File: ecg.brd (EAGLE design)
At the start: 56 x 85 mm, 1 part

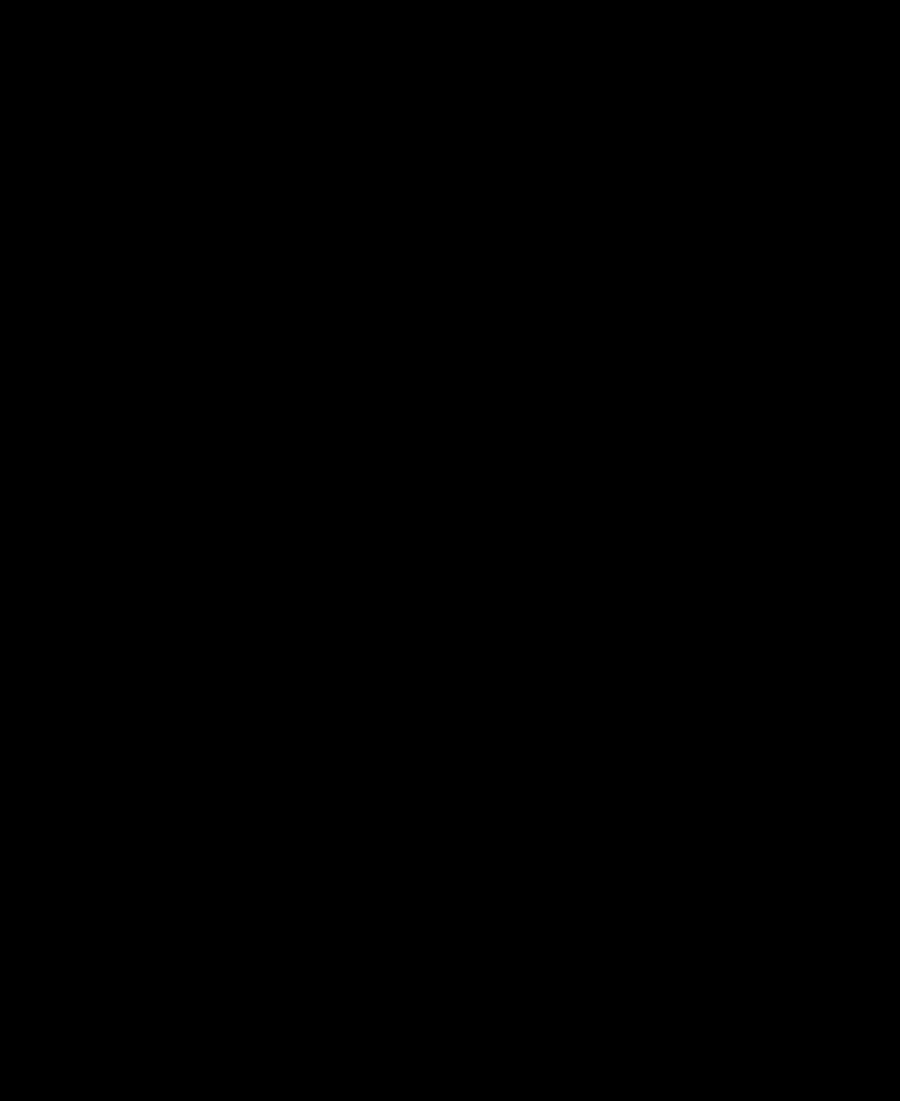
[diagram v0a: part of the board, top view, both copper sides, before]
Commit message: Added TMP102 and ADAS1000 to schematics
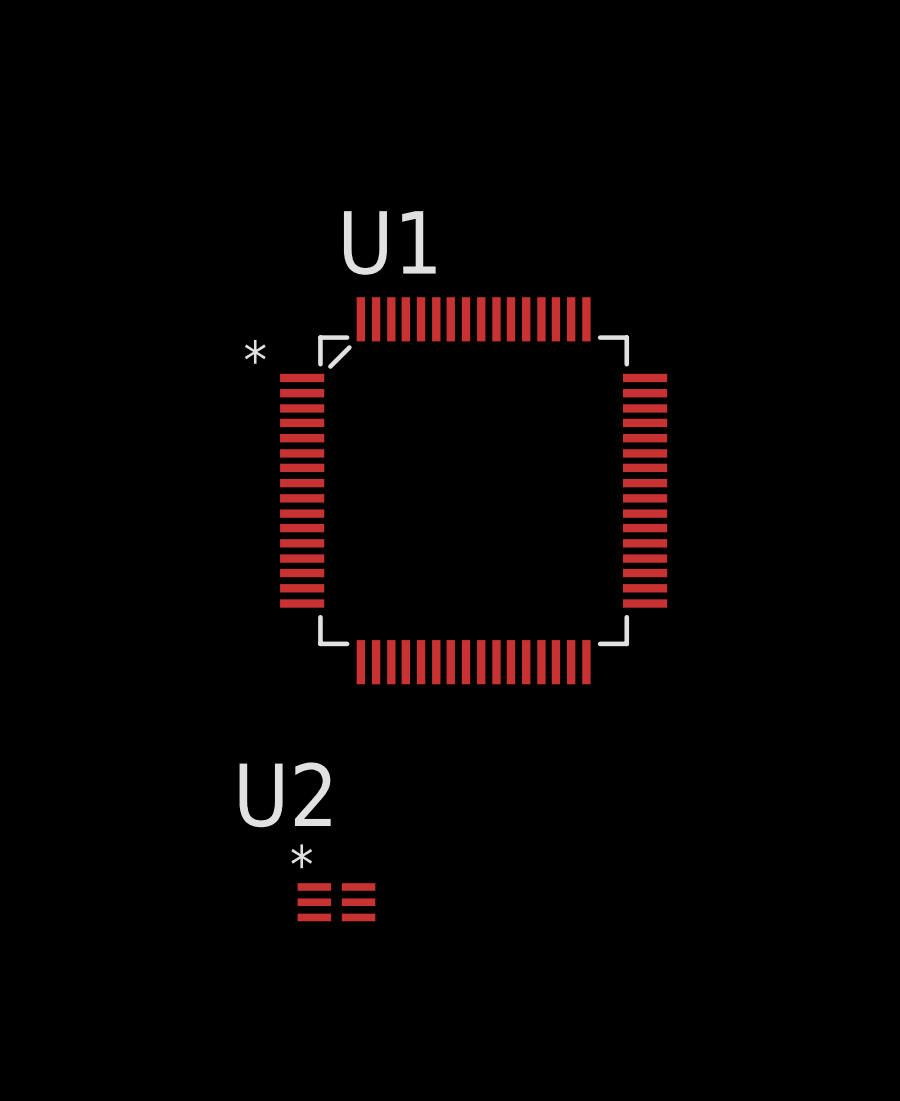
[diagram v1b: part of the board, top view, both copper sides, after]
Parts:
- added U1: ADAS1000-2BSTZ, ADAS1000:QFN50P1200X1200X160-64N
- added U2: TMP102AIDRLT, TMP102:SOT50P160X60-6N
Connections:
- new net !PD: U1.53
- new net ADCVDD: U1.26
- new net ADCVDD_2: U1.55
- new net AVDD: U1.58
- new net AVDD_2: U1.18
- new net AVDD_3: U1.63
- new net AVDD_4: U1.23
- new net DVDD: U1.51
- new net DVDD_2: U1.30
- new net IOVDD: U1.46
- new net IOVDD_2: U1.35
- new net V+: U2.5
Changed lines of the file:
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@@
 <elements>
 <element name="U$1" library="microbuilder" package="RASBERRYPI_SHIELD" value="RASPBERRYPI_BB" x="0" y="0"/>
+<element name="U1" library="ADAS1000" package="QFN50P1200X1200X160-64N" value="ADAS1000-2BSTZ" x="23.114" y="54.356">
+<attribute name="PACKAGE" value="LQFP-64" x="23.114" y="54.356" size="1.778" layer="27" display="off"/>
+<attribute name="OC_NEWARK" value="52W9262" x="23.114" y="54.356" size="1.778" layer="27" display="off"/>
+<attribute name="MPN" value="ADAS1000-2BSTZ " x="23.114" y="54.356" size="1.778" layer="27" display="off"/>
+<attribute name="SUPPLIER" value="ANALOG DEVICES " x="23.114" y="54.356" size="1.778" layer="27" display="off"/>
+<attribute name="OC_FARNELL" value="2254936" x="23.114" y="54.356" size="1.778" layer="27" display="off"/>
+</element>
+<element name="U2" library="TMP102" package="SOT50P160X60-6N" value="TMP102AIDRLT" x="18.542" y="40.64">
+<attribute name="PACKAGE" value="SOT-23-6" x="18.542" y="40.64" size="1.778" layer="27" display="off"/>
+<attribute name="OC_NEWARK" value="53M3987" x="18.542" y="40.64" size="1.778" layer="27" display="off"/>
+<attribute name="MPN" value="TMP102AIDRLT" x="18.542" y="40.64" size="1.778" layer="27" display="off"/>
+<attribute name="SUPPLIER" value="Texas Instruments" x="18.542" y="40.64" size="1.778" layer="27" display="off"/>
+<attribute name="OC_FARNELL" value="1652477" x="18.542" y="40.64" size="1.778" layer="27" display="off"/>
+</element>
 </elements>
 <signals>
+<signal name="AVDD_2">
+<contactref element="U1" pad="18"/>
+</signal>
+<signal name="AVDD_3">
+<contactref element="U1" pad="63"/>
+</signal>
+<signal name="AVDD_4">
+<contactref element="U1" pad="23"/>
+</signal>
+<signal name="AVDD">
+<contactref element="U1" pad="58"/>
+</signal>
+<signal name="DVDD_2">
+<contactref element="U1" pad="30"/>
+</signal>
+<signal name="DVDD">
+<contactref element="U1" pad="51"/>
+</signal>
+<signal name="ADCVDD_2">
+<contactref element="U1" pad="55"/>
+</signal>
+<signal name="ADCVDD">
+<contactref element="U1" pad="26"/>
+</signal>
+<signal name="IOVDD_2">
+<contactref element="U1" pad="35"/>
+</signal>
+<signal name="IOVDD">
+<contactref element="U1" pad="46"/>
+</signal>
+<signal name="!PD">
+<contactref element="U1" pad="53"/>
+</signal>
+<signal name="V+">
+<contactref element="U2" pad="5"/>
+</signal>
 </signals>
 <errors>
